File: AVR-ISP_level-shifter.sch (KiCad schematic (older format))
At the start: 24 parts, among them Q1 BSS138, Q2 BSS138, Q3 BSS138, Q4 BSS138, Q5 BSS138, Q6 BSS138, Q7 BSS138, Q8 BSS138, SW1 APEM 25439NH, U1 AMS1117-3.3

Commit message: Schematic + footprint assignation might be done.
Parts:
- C1, C2: footprint my_parts:MADW__C0805 -> Capacitors_SMD:C_0603_HandSoldering
- INPUT2, OUTPUT2: footprint AVR-ISP-10 -> DIL-Headers:DIL-5
- SW1: footprint (none) -> Switches:switch_vert_SPDT_ON-OFF-ON_TH_APEM-25439NH
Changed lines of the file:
@@
 F 0 "INPUT2" H 6650 2450 50  0000 C CNN
 F 1 "AVR-ISP-10" H 6410 1770 50  0000 L BNN
-F 2 "AVR-ISP-10" V 6000 2150 50  0001 C CNN
+F 2 "DIL-Headers:DIL-5" V 6000 2150 50  0001 C CNN
 F 3 "" H 6750 2100 60  0000 C CNN
 	1    6750 2100
@@
 F 0 "OUTPUT2" H 6650 4250 50  0000 C CNN
 F 1 "AVR-ISP-10" H 6410 3570 50  0000 L BNN
-F 2 "AVR-ISP-10" V 6000 3950 50  0001 C CNN
+F 2 "DIL-Headers:DIL-5" V 6000 3950 50  0001 C CNN
 F 3 "" H 6750 3900 60  0000 C CNN
 	1    6750 3900
@@
 F 0 "SW1" H 3551 3600 50  0000 C CNN
 F 1 "APEM 25439NH" H 3500 3300 50  0000 C CNN
-F 2 "" H 3750 3450 60  0001 C CNN
+F 2 "Switches:switch_vert_SPDT_ON-OFF-ON_TH_APEM-25439NH" H 3750 3450 60  0001 C CNN
 F 3 "" H 3750 3450 60  0000 C CNN
 	1    3750 3450
@@
 F 0 "C1" H 3325 1800 50  0000 L CNN
 F 1 "1µF" H 3325 1600 50  0000 L CNN
-F 2 "my_parts:MADW__C0805" H 3338 1550 30  0001 C CNN
+F 2 "Capacitors_SMD:C_0603_HandSoldering" H 3338 1550 30  0001 C CNN
 F 3 "" H 3300 1700 60  0000 C CNN
 	1    3300 1700
@@
 F 0 "C2" H 4425 1800 50  0000 L CNN
 F 1 "1µF" H 4425 1600 50  0000 L CNN
-F 2 "my_parts:MADW__C0805" H 4438 1550 30  0001 C CNN
+F 2 "Capacitors_SMD:C_0603_HandSoldering" H 4438 1550 30  0001 C CNN
 F 3 "" H 4400 1700 60  0000 C CNN
 	1    4400 1700

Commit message: Changed a few footprints.
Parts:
- Q1, Q2, Q3, Q4, Q5, Q6, Q7, Q8: footprint my_parts:MADW__SOT23 -> Housings_SOT-23_SOT-143_TSOT-6:SOT-23
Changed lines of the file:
@@
 F 0 "U1" H 3850 2050 60  0000 C CNN
 F 1 "AMS1117-3.3" H 3550 1950 60  0000 L CNN
-F 2 "SMD_Packages:SOT-223" H 3850 1650 60  0001 C CNN
+F 2 "SMD_Packages:SOT-223" H 3850 2150 20  0000 C CNN
 F 3 "" H 3850 1650 60  0000 C CNN
 	1    3850 1650
@@
 F 0 "Q1" V 9050 1600 50  0000 L CNN
 F 1 "BSS138" V 9450 1400 50  0000 L CNN
-F 2 "my_parts:MADW__SOT23" V 9550 1400 39  0000 L CIN
+F 2 "Housings_SOT-23_SOT-143_TSOT-6:SOT-23" V 9550 1400 20  0000 L CIN
 F 3 "" H 9200 1550 50  0000 L CNN
 	1    9200 1550
@@
 F 0 "Q2" V 9550 1600 50  0000 L CNN
 F 1 "BSS138" V 9950 1400 50  0000 L CNN
-F 2 "my_parts:MADW__SOT23" V 10050 1400 39  0000 L CIN
+F 2 "Housings_SOT-23_SOT-143_TSOT-6:SOT-23" V 10050 1400 20  0001 L CIN
 F 3 "" H 9700 1550 50  0000 L CNN
 	1    9700 1550
@@
 F 0 "Q3" V 9050 2400 50  0000 L CNN
 F 1 "BSS138" V 9450 2200 50  0000 L CNN
-F 2 "my_parts:MADW__SOT23" V 9550 2200 39  0000 L CIN
+F 2 "Housings_SOT-23_SOT-143_TSOT-6:SOT-23" V 9550 2200 20  0001 L CIN
 F 3 "" H 9200 2350 50  0000 L CNN
 	1    9200 2350
@@
 F 0 "Q4" V 9550 2400 50  0000 L CNN
 F 1 "BSS138" V 9950 2200 50  0000 L CNN
-F 2 "my_parts:MADW__SOT23" V 10050 2200 39  0000 L CIN
+F 2 "Housings_SOT-23_SOT-143_TSOT-6:SOT-23" V 10050 2200 20  0001 L CIN
 F 3 "" H 9700 2350 50  0000 L CNN
 	1    9700 2350
@@
 F 0 "Q5" V 9050 3200 50  0000 L CNN
 F 1 "BSS138" V 9450 3000 50  0000 L CNN
-F 2 "my_parts:MADW__SOT23" V 9550 3000 39  0000 L CIN
+F 2 "Housings_SOT-23_SOT-143_TSOT-6:SOT-23" V 9550 3000 20  0001 L CIN
 F 3 "" H 9200 3150 50  0000 L CNN
 	1    9200 3150
@@
 F 0 "Q6" V 9550 3200 50  0000 L CNN
 F 1 "BSS138" V 9950 3000 50  0000 L CNN
-F 2 "my_parts:MADW__SOT23" V 10050 3000 39  0000 L CIN
+F 2 "Housings_SOT-23_SOT-143_TSOT-6:SOT-23" V 10050 3000 20  0001 L CIN
 F 3 "" H 9700 3150 50  0000 L CNN
 	1    9700 3150
@@
 F 0 "SW1" H 3551 3600 50  0000 C CNN
 F 1 "APEM 25439NH" H 3500 3300 50  0000 C CNN
-F 2 "Switches:switch_vert_SPDT_ON-OFF-ON_TH_APEM-25439NH" H 3750 3450 60  0001 C CNN
+F 2 "Switches:switch_vert_SPDT_ON-OFF-ON_TH_APEM-25439NH" H 3750 3200 20  0000 C CNN
 F 3 "" H 3750 3450 60  0000 C CNN
 	1    3750 3450
@@
 F 0 "Q7" V 9050 4000 50  0000 L CNN
 F 1 "BSS138" V 9450 3800 50  0000 L CNN
-F 2 "my_parts:MADW__SOT23" V 9550 3800 39  0000 L CIN
+F 2 "Housings_SOT-23_SOT-143_TSOT-6:SOT-23" V 9550 3800 20  0001 L CIN
 F 3 "" H 9200 3950 50  0000 L CNN
 	1    9200 3950
@@
 F 0 "Q8" V 9550 4000 50  0000 L CNN
 F 1 "BSS138" V 9950 3800 50  0000 L CNN
-F 2 "my_parts:MADW__SOT23" V 10050 3800 39  0000 L CIN
+F 2 "Housings_SOT-23_SOT-143_TSOT-6:SOT-23" V 10050 3800 20  0001 L CIN
 F 3 "" H 9700 3950 50  0000 L CNN
 	1    9700 3950

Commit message: Might be done!
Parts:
- C1, C2: footprint Capacitors_SMD:C_0603_HandSoldering -> Capacitors_SMD:C_0603
- R1, R2, R3, R4: footprint Resistors_SMD:R_0603_HandSoldering -> Resistors_SMD:R_0603
- R5: renamed from R7; footprint Resistors_SMD:R_0603_HandSoldering -> Resistors_SMD:R_0603
- R6: renamed from R8; footprint Resistors_SMD:R_0603_HandSoldering -> Resistors_SMD:R_0603
- R7: renamed from R9; footprint Resistors_SMD:R_0603_HandSoldering -> Resistors_SMD:R_0603
- R8: renamed from R10; footprint Resistors_SMD:R_0603_HandSoldering -> Resistors_SMD:R_0603
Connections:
- net MISO_PRG: now also Q1.2 (S), R1.2; no longer Q3.2 (S), R3.2
- net MISO_TARGET: now also Q2.2 (S), R2.2; no longer Q4.2 (S), R4.2
- net MOSI_PRG: now also Q7.2 (S), R7.2; no longer Q1.2 (S), R1.2
- net MOSI_TARGET: now also Q8.2 (S), R8.2; no longer Q2.2 (S), R2.2
- net RESET_PRG: now also Q5.2 (S), R5.2; no longer Q7.2 (S), R7.2
- net RESET_TARGET: now also Q6.2 (S), R6.2; no longer Q8.2 (S), R8.2
- net SCK_PRG: now also Q3.2 (S), R3.2; no longer Q5.2 (S), R5.2
- net SCK_TARGET: now also Q4.2 (S), R4.2; no longer Q6.2 (S), R6.2
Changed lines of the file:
@@
 F 0 "R2" V 10030 1450 50  0000 C CNN
 F 1 "1K5" V 9950 1450 50  0000 C CNN
-F 2 "Resistors_SMD:R_0603_HandSoldering" V 9880 1450 30  0001 C CNN
+F 2 "Resistors_SMD:R_0603" V 9880 1450 30  0001 C CNN
 F 3 "" H 9950 1450 30  0000 C CNN
 	1    9950 1450
@@
 F 0 "R1" V 9030 1450 50  0000 C CNN
 F 1 "1K5" V 8950 1450 50  0000 C CNN
-F 2 "Resistors_SMD:R_0603_HandSoldering" V 8880 1450 30  0001 C CNN
+F 2 "Resistors_SMD:R_0603" V 8880 1450 30  0001 C CNN
 F 3 "" H 8950 1450 30  0000 C CNN
 	1    8950 1450
@@
 F 0 "R4" V 10030 2250 50  0000 C CNN
 F 1 "1K5" V 9950 2250 50  0000 C CNN
-F 2 "Resistors_SMD:R_0603_HandSoldering" V 9880 2250 30  0001 C CNN
+F 2 "Resistors_SMD:R_0603" V 9880 2250 30  0001 C CNN
 F 3 "" H 9950 2250 30  0000 C CNN
 	1    9950 2250
@@
 F 0 "R3" V 9030 2250 50  0000 C CNN
 F 1 "1K5" V 8950 2250 50  0000 C CNN
-F 2 "Resistors_SMD:R_0603_HandSoldering" V 8880 2250 30  0001 C CNN
+F 2 "Resistors_SMD:R_0603" V 8880 2250 30  0001 C CNN
 F 3 "" H 8950 2250 30  0000 C CNN
 	1    8950 2250
@@
 $EndComp
 $Comp
-L R R8
+L R R6
 U 1 1 55339F9A
 P 9950 3050
-F 0 "R8" V 10030 3050 50  0000 C CNN
+F 0 "R6" V 10030 3050 50  0000 C CNN
 F 1 "1K5" V 9950 3050 50  0000 C CNN
-F 2 "Resistors_SMD:R_0603_HandSoldering" V 9880 3050 30  0001 C CNN
+F 2 "Resistors_SMD:R_0603" V 9880 3050 30  0001 C CNN
 F 3 "" H 9950 3050 30  0000 C CNN
 	1    9950 3050
@@
 $EndComp
 $Comp
-L R R7
+L R R5
 U 1 1 55339FA0
 P 8950 3050
-F 0 "R7" V 9030 3050 50  0000 C CNN
+F 0 "R5" V 9030 3050 50  0000 C CNN
 F 1 "1K5" V 8950 3050 50  0000 C CNN
-F 2 "Resistors_SMD:R_0603_HandSoldering" V 8880 3050 30  0001 C CNN
+F 2 "Resistors_SMD:R_0603" V 8880 3050 30  0001 C CNN
 F 3 "" H 8950 3050 30  0000 C CNN
 	1    8950 3050
@@
 "A-OFF-B"
 Text Label 8800 1650 2    60   ~ 0
+MISO_PRG
+Text Label 8800 2450 2    60   ~ 0
+SCK_PRG
+Text Label 8800 3250 2    60   ~ 0
+RESET_PRG
+Text Label 8800 4050 2    60   ~ 0
 MOSI_PRG
-Text Label 8800 2450 2    60   ~ 0
-MISO_PRG
-Text Label 8800 3250 2    60   ~ 0
-SCK_PRG
-Text Label 8800 4050 2    60   ~ 0
-RESET_PRG
 $Comp
 L BSS138 Q7
@@
 $EndComp
 $Comp
-L R R10
+L R R8
 U 1 1 55339C16
 P 9950 3850
-F 0 "R10" V 10030 3850 50  0000 C CNN
+F 0 "R8" V 10030 3850 50  0000 C CNN
 F 1 "1K5" V 9950 3850 50  0000 C CNN
-F 2 "Resistors_SMD:R_0603_HandSoldering" V 9880 3850 30  0001 C CNN
+F 2 "Resistors_SMD:R_0603" V 9880 3850 30  0001 C CNN
 F 3 "" H 9950 3850 30  0000 C CNN
 	1    9950 3850
@@
 $EndComp
 $Comp
-L R R9
+L R R7
 U 1 1 55339C1C
 P 8950 3850
-F 0 "R9" V 9030 3850 50  0000 C CNN
+F 0 "R7" V 9030 3850 50  0000 C CNN
 F 1 "1K5" V 8950 3850 50  0000 C CNN
-F 2 "Resistors_SMD:R_0603_HandSoldering" V 8880 3850 30  0001 C CNN
+F 2 "Resistors_SMD:R_0603" V 8880 3850 30  0001 C CNN
 F 3 "" H 8950 3850 30  0000 C CNN
 	1    8950 3850
@@
 $EndComp
 Text Label 10100 1650 0    60   ~ 0
+MISO_TARGET
+Text Label 10100 2450 0    60   ~ 0
+SCK_TARGET
+Text Label 10100 3250 0    60   ~ 0
+RESET_TARGET
+Text Label 10100 4050 0    60   ~ 0
 MOSI_TARGET
-Text Label 10100 2450 0    60   ~ 0
-MISO_TARGET
-Text Label 10100 3250 0    60   ~ 0
-SCK_TARGET
-Text Label 10100 4050 0    60   ~ 0
-RESET_TARGET
 Text Label 8800 1250 2    60   ~ 0
 VCC_PRG
@@
 F 0 "C1" H 3325 1800 50  0000 L CNN
 F 1 "1µF" H 3325 1600 50  0000 L CNN
-F 2 "Capacitors_SMD:C_0603_HandSoldering" H 3338 1550 30  0001 C CNN
+F 2 "Capacitors_SMD:C_0603" H 3338 1550 30  0001 C CNN
 F 3 "" H 3300 1700 60  0000 C CNN
 	1    3300 1700
@@
 F 0 "C2" H 4425 1800 50  0000 L CNN
 F 1 "1µF" H 4425 1600 50  0000 L CNN
-F 2 "Capacitors_SMD:C_0603_HandSoldering" H 4438 1550 30  0001 C CNN
+F 2 "Capacitors_SMD:C_0603" H 4438 1550 30  0001 C CNN
 F 3 "" H 4400 1700 60  0000 C CNN
 	1    4400 1700

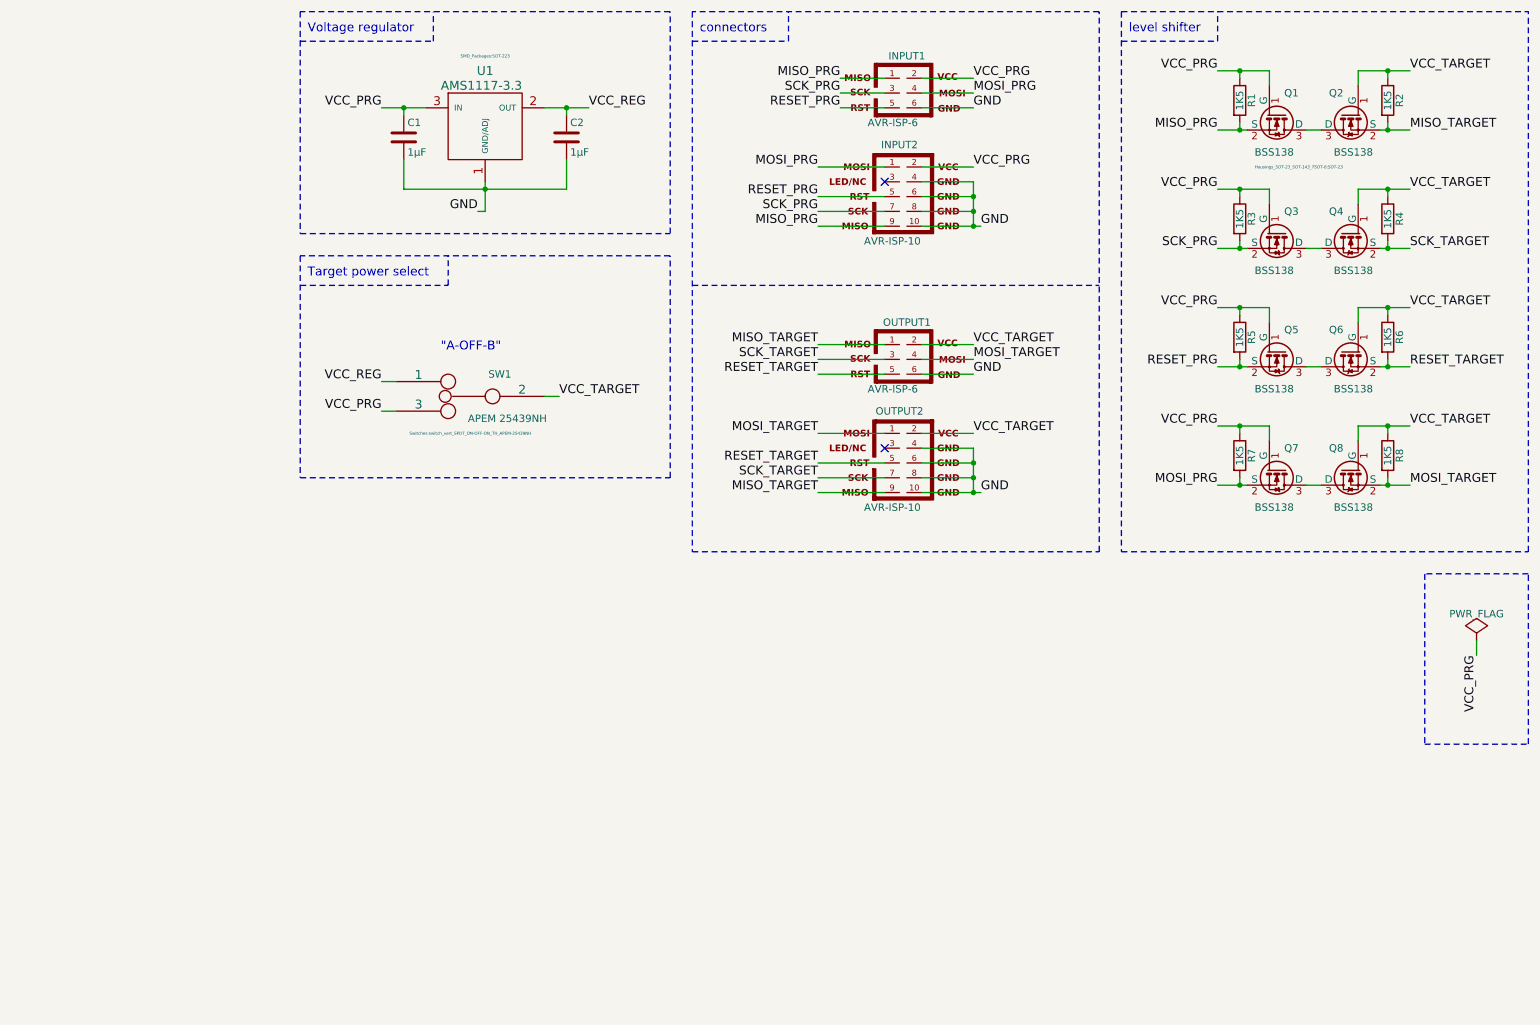
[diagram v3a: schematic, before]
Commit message: Added comment to schematic + silkscreen tweaks.
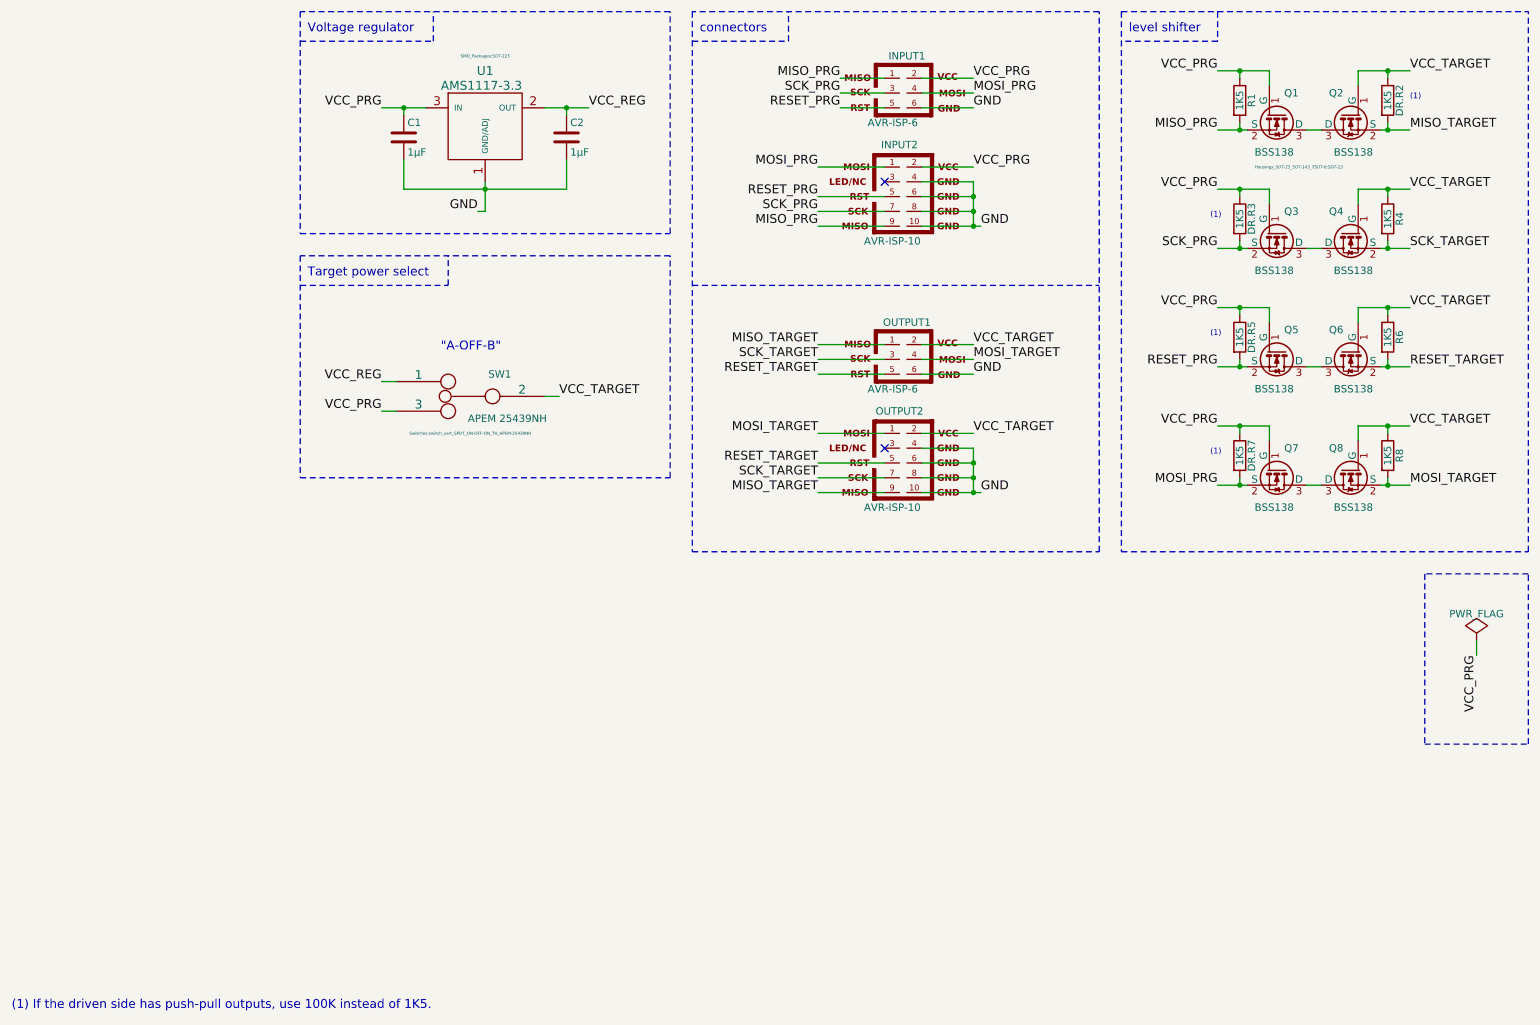
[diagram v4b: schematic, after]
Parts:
- renumbered R2 to DR.R2, R3 to DR.R3, R5 to DR.R5, R7 to DR.R7
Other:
- note added: "(1)"
- note added: "(1) If the driven side has push-pull outputs, use 100K instead of 1K5."
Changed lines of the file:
@@
 Sheet 1 1
 Title "AVR-ISP_level-shifter"
-Date "Sun 19 Apr 2015"
-Rev "0.1"
+Date "Fri 24 Apr 2015"
+Rev "0.11"
 Comp "2015 - blog.spitzenpfeil.org"
 Comment1 ""
@@
 $EndComp
 $Comp
-L R R2
+L R DR.R2
 U 1 1 55339929
 P 9950 1450
-F 0 "R2" V 10030 1450 50  0000 C CNN
+F 0 "DR.R2" V 10030 1450 50  0000 C CNN
 F 1 "1K5" V 9950 1450 50  0000 C CNN
 F 2 "Resistors_SMD:R_0603" V 9880 1450 30  0001 C CNN
@@
 $EndComp
 $Comp
-L R R3
+L R DR.R3
 U 1 1 55339C56
 P 8950 2250
-F 0 "R3" V 9030 2250 50  0000 C CNN
+F 0 "DR.R3" V 9030 2250 50  0000 C CNN
 F 1 "1K5" V 8950 2250 50  0000 C CNN
 F 2 "Resistors_SMD:R_0603" V 8880 2250 30  0001 C CNN
@@
 $EndComp
 $Comp
-L R R5
+L R DR.R5
 U 1 1 55339FA0
 P 8950 3050
-F 0 "R5" V 9030 3050 50  0000 C CNN
+F 0 "DR.R5" V 9030 3050 50  0000 C CNN
 F 1 "1K5" V 8950 3050 50  0000 C CNN
 F 2 "Resistors_SMD:R_0603" V 8880 3050 30  0001 C CNN
@@
 $EndComp
 $Comp
-L R R7
+L R DR.R7
 U 1 1 55339C1C
 P 8950 3850
-F 0 "R7" V 9030 3850 50  0000 C CNN
+F 0 "DR.R7" V 9030 3850 50  0000 C CNN
 F 1 "1K5" V 8950 3850 50  0000 C CNN
 F 2 "Resistors_SMD:R_0603" V 8880 3850 30  0001 C CNN
@@
 Text Label 8800 3650 2    60   ~ 0
 VCC_PRG
-Text Notes 8200 1000 0    60   ~ 0
-level shifter
 Text Label 7150 1500 0    60   ~ 0
 GND
@@
 Wire Notes Line
 	8150 850  10900 850
-Wire Notes Line
-	8150 1050 8800 1050
-Wire Notes Line
-	8800 1050 8800 850
 Wire Wire Line
 	6800 1500 7150 1500
@@
 Wire Notes Line
 	3600 2700 3600 2500
+Text Notes 650  7600 0    60   ~ 0
+(1) If the driven side has push-pull outputs, use 100K instead of 1K5.
+Text Notes 8200 1000 0    60   ~ 0
+level shifter
+Wire Notes Line
+	8800 850  8800 1050
+Wire Notes Line
+	8800 1050 8150 1050
+Text Notes 10100 1450 0    39   ~ 0
+(1)
+Text Notes 8750 2250 0    39   ~ 0
+(1)
+Text Notes 8750 3050 0    39   ~ 0
+(1)
+Text Notes 8750 3850 0    39   ~ 0
+(1)
 $EndSCHEMATC

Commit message: Added load resistor (~300R) to pull minimum load current out of 3.3V LDO.
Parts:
- added R9: 300R, Resistors_SMD:R_0603, symbol R
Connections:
- net GND: now also R9.2
- net VCC_REG: now also R9.1
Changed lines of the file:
@@
 Sheet 1 1
 Title "AVR-ISP_level-shifter"
-Date "Fri 24 Apr 2015"
-Rev "0.11"
+Date "Tue 05 May 2015"
+Rev "0.12"
 Comp "2015 - blog.spitzenpfeil.org"
 Comment1 ""
@@
 Text Label 4350 3450 0    60   ~ 0
 VCC_TARGET
-Text Label 4550 1500 0    60   ~ 0
+Text Label 4400 1300 0    60   ~ 0
 VCC_REG
 $Comp
@@
 	3300 1850 3300 2050
 Wire Wire Line
-	3300 2050 4400 2050
+	3300 2050 4650 2050
 Connection ~ 3850 2050
 Wire Wire Line
@@
 	3850 2200 3800 2200
 Wire Wire Line
-	4400 1500 4400 1550
+	4400 1300 4400 1550
 Wire Wire Line
 	3300 1500 3300 1550
 Connection ~ 4400 1500
 Connection ~ 3300 1500
-Wire Wire Line
-	4250 1500 4550 1500
 $Comp
 L PWR_FLAG #FLG01
@@
 Text Notes 8750 3850 0    39   ~ 0
 (1)
+$Comp
+L R R9
+U 1 1 5548E9BF
+P 4650 1700
+F 0 "R9" V 4730 1700 50  0000 C CNN
+F 1 "300R" V 4650 1700 50  0000 C CNN
+F 2 "Resistors_SMD:R_0603" V 4580 1700 30  0001 C CNN
+F 3 "" H 4650 1700 30  0000 C CNN
+	1    4650 1700
+	1    0    0    -1
+$EndComp
+Wire Wire Line
+	4650 2050 4650 1850
+Connection ~ 4400 2050
+Wire Wire Line
+	4250 1500 4650 1500
+Wire Wire Line
+	4650 1500 4650 1550
 $EndSCHEMATC

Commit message: Changed footprints for easier handsoldering + necessary tweaks.
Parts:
- C1, C2: footprint Capacitors_SMD:C_0603 -> Capacitors_SMD:C_0805
- DR.R2, DR.R3, DR.R5, DR.R7, R1, R4, R6, R8, R9: footprint Resistors_SMD:R_0603 -> Resistors_SMD:R_0603_HandSoldering
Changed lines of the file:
@@
 F 0 "DR.R2" V 10030 1450 50  0000 C CNN
 F 1 "1K5" V 9950 1450 50  0000 C CNN
-F 2 "Resistors_SMD:R_0603" V 9880 1450 30  0001 C CNN
+F 2 "Resistors_SMD:R_0603_HandSoldering" V 9880 1450 30  0001 C CNN
 F 3 "" H 9950 1450 30  0000 C CNN
 	1    9950 1450
@@
 F 0 "R1" V 9030 1450 50  0000 C CNN
 F 1 "1K5" V 8950 1450 50  0000 C CNN
-F 2 "Resistors_SMD:R_0603" V 8880 1450 30  0001 C CNN
+F 2 "Resistors_SMD:R_0603_HandSoldering" V 8880 1450 30  0001 C CNN
 F 3 "" H 8950 1450 30  0000 C CNN
 	1    8950 1450
@@
 F 0 "R4" V 10030 2250 50  0000 C CNN
 F 1 "1K5" V 9950 2250 50  0000 C CNN
-F 2 "Resistors_SMD:R_0603" V 9880 2250 30  0001 C CNN
+F 2 "Resistors_SMD:R_0603_HandSoldering" V 9880 2250 30  0001 C CNN
 F 3 "" H 9950 2250 30  0000 C CNN
 	1    9950 2250
@@
 F 0 "DR.R3" V 9030 2250 50  0000 C CNN
 F 1 "1K5" V 8950 2250 50  0000 C CNN
-F 2 "Resistors_SMD:R_0603" V 8880 2250 30  0001 C CNN
+F 2 "Resistors_SMD:R_0603_HandSoldering" V 8880 2250 30  0001 C CNN
 F 3 "" H 8950 2250 30  0000 C CNN
 	1    8950 2250
@@
 F 0 "R6" V 10030 3050 50  0000 C CNN
 F 1 "1K5" V 9950 3050 50  0000 C CNN
-F 2 "Resistors_SMD:R_0603" V 9880 3050 30  0001 C CNN
+F 2 "Resistors_SMD:R_0603_HandSoldering" V 9880 3050 30  0001 C CNN
 F 3 "" H 9950 3050 30  0000 C CNN
 	1    9950 3050
@@
 F 0 "DR.R5" V 9030 3050 50  0000 C CNN
 F 1 "1K5" V 8950 3050 50  0000 C CNN
-F 2 "Resistors_SMD:R_0603" V 8880 3050 30  0001 C CNN
+F 2 "Resistors_SMD:R_0603_HandSoldering" V 8880 3050 30  0001 C CNN
 F 3 "" H 8950 3050 30  0000 C CNN
 	1    8950 3050
@@
 F 0 "R8" V 10030 3850 50  0000 C CNN
 F 1 "1K5" V 9950 3850 50  0000 C CNN
-F 2 "Resistors_SMD:R_0603" V 9880 3850 30  0001 C CNN
+F 2 "Resistors_SMD:R_0603_HandSoldering" V 9880 3850 30  0001 C CNN
 F 3 "" H 9950 3850 30  0000 C CNN
 	1    9950 3850
@@
 F 0 "DR.R7" V 9030 3850 50  0000 C CNN
 F 1 "1K5" V 8950 3850 50  0000 C CNN
-F 2 "Resistors_SMD:R_0603" V 8880 3850 30  0001 C CNN
+F 2 "Resistors_SMD:R_0603_HandSoldering" V 8880 3850 30  0001 C CNN
 F 3 "" H 8950 3850 30  0000 C CNN
 	1    8950 3850
@@
 F 0 "C1" H 3325 1800 50  0000 L CNN
 F 1 "1µF" H 3325 1600 50  0000 L CNN
-F 2 "Capacitors_SMD:C_0603" H 3338 1550 30  0001 C CNN
+F 2 "Capacitors_SMD:C_0805" H 3338 1550 30  0001 C CNN
 F 3 "" H 3300 1700 60  0000 C CNN
 	1    3300 1700
@@
 F 0 "C2" H 4425 1800 50  0000 L CNN
 F 1 "1µF" H 4425 1600 50  0000 L CNN
-F 2 "Capacitors_SMD:C_0603" H 4438 1550 30  0001 C CNN
+F 2 "Capacitors_SMD:C_0805" H 4438 1550 30  0001 C CNN
 F 3 "" H 4400 1700 60  0000 C CNN
 	1    4400 1700
@@
 F 0 "R9" V 4730 1700 50  0000 C CNN
 F 1 "300R" V 4650 1700 50  0000 C CNN
-F 2 "Resistors_SMD:R_0603" V 4580 1700 30  0001 C CNN
+F 2 "Resistors_SMD:R_0603_HandSoldering" V 4580 1700 30  0001 C CNN
 F 3 "" H 4650 1700 30  0000 C CNN
 	1    4650 1700
